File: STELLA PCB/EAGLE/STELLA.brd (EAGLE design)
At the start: 13.2 x 13.2 mm, 51 parts, among them Q1 ECS-.327-5-16-TR, T1 NXP_60_2N7002BKM, T2 NXP_60_2N7002BKM, T3 NXP_60_2N7002BKM, U1 PSSI2021SAY, U10 AD5142BCPZ100, U2 PSSI2021SAY, U4 SN74AUP1G06, U5 SN74AUP1G06, U6 MAX17220ENT+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

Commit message: update
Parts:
- C1, C2: value 4.7uF -> 4.7uF/6.3VDC
- C10, C3, C5, C7, C8, C9: value 0.1uF -> 0.1uF/6.3VDC
- C6, C6A: value 100uF -> 100uF/6.3VDC
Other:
- board text added: "1 - 8: Extension bus (optional)"
- board text removed: "1 - 8: Extension bus (nur optional)"
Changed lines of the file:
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@@
 <?xml version="1.0" encoding="utf-8"?>
 <!DOCTYPE eagle SYSTEM "eagle.dtd">
-<eagle version="9.4.2">
+<eagle version="9.6.2">
 <drawing>
 <settings>
@@
 <layers>
 <layer number="1" name="Top" color="4" fill="1" visible="yes" active="yes"/>
-<layer number="2" name="Route2" color="1" fill="3" visible="yes" active="yes"/>
-<layer number="3" name="Route3" color="4" fill="3" visible="yes" active="yes"/>
+<layer number="2" name="Route2" color="1" fill="3" visible="no" active="yes"/>
+<layer number="3" name="Route3" color="4" fill="3" visible="no" active="yes"/>
 <layer number="4" name="Route4" color="1" fill="4" visible="no" active="no"/>
 <layer number="5" name="Route5" color="4" fill="4" visible="no" active="no"/>
@@
 <layer number="24" name="bOrigins" color="15" fill="1" visible="yes" active="yes"/>
 <layer number="25" name="tNames" color="7" fill="1" visible="yes" active="yes"/>
-<layer number="26" name="bNames" color="7" fill="1" visible="yes" active="yes"/>
-<layer number="27" name="tValues" color="7" fill="1" visible="yes" active="yes"/>
-<layer number="28" name="bValues" color="7" fill="1" visible="yes" active="yes"/>
-<layer number="29" name="tStop" color="7" fill="3" visible="yes" active="yes"/>
-<layer number="30" name="bStop" color="7" fill="6" visible="yes" active="yes"/>
-<layer number="31" name="tCream" color="7" fill="4" visible="yes" active="yes"/>
-<layer number="32" name="bCream" color="7" fill="5" visible="yes" active="yes"/>
+<layer number="26" name="bNames" color="7" fill="1" visible="no" active="yes"/>
+<layer number="27" name="tValues" color="7" fill="1" visible="no" active="yes"/>
+<layer number="28" name="bValues" color="7" fill="1" visible="no" active="yes"/>
+<layer number="29" name="tStop" color="7" fill="3" visible="no" active="yes"/>
+<layer number="30" name="bStop" color="7" fill="6" visible="no" active="yes"/>
+<layer number="31" name="tCream" color="7" fill="4" visible="no" active="yes"/>
+<layer number="32" name="bCream" color="7" fill="5" visible="no" active="yes"/>
 <layer number="33" name="tFinish" color="6" fill="3" visible="no" active="yes"/>
 <layer number="34" name="bFinish" color="6" fill="6" visible="no" active="yes"/>
 <layer number="35" name="tGlue" color="7" fill="4" visible="no" active="yes"/>
 <layer number="36" name="bGlue" color="7" fill="5" visible="no" active="yes"/>
-<layer number="37" name="tTest" color="7" fill="1" visible="yes" active="yes"/>
-<layer number="38" name="bTest" color="7" fill="1" visible="yes" active="yes"/>
+<layer number="37" name="tTest" color="7" fill="1" visible="no" active="yes"/>
+<layer number="38" name="bTest" color="7" fill="1" visible="no" active="yes"/>
 <layer number="39" name="tKeepout" color="4" fill="11" visible="no" active="yes"/>
 <layer number="40" name="bKeepout" color="1" fill="11" visible="no" active="yes"/>
@@
 <layer number="42" name="bRestrict" color="1" fill="10" visible="no" active="yes"/>
 <layer number="43" name="vRestrict" color="2" fill="10" visible="no" active="yes"/>
-<layer number="44" name="Drills" color="7" fill="1" visible="yes" active="yes"/>
-<layer number="45" name="Holes" color="7" fill="1" visible="yes" active="yes"/>
-<layer number="46" name="Milling" color="3" fill="1" visible="yes" active="yes"/>
-<layer number="47" name="Measures" color="7" fill="1" visible="yes" active="yes"/>
+<layer number="44" name="Drills" color="7" fill="1" visible="no" active="yes"/>
+<layer number="45" name="Holes" color="7" fill="1" visible="no" active="yes"/>
+<layer number="46" name="Milling" color="3" fill="1" visible="no" active="yes"/>
+<layer number="47" name="Measures" color="7" fill="1" visible="no" active="yes"/>
 <layer number="48" name="Document" color="7" fill="1" visible="yes" active="yes"/>
 <layer number="49" name="Reference" color="7" fill="1" visible="yes" active="yes"/>
@@
 <text x="-10.55" y="-2.2" size="1.016" layer="105">16</text>
 <text x="-10.575" y="-3.5" size="1.016" layer="105">17</text>
-<text x="-19.4" y="-8.95" size="1.016" layer="105">1 - 8: Extension bus (nur optional)</text>
+<text x="-19.4" y="-8.95" size="1.016" layer="105">1 - 8: Extension bus (optional)</text>
 <text x="-19.55" y="-11.15" size="1.016" layer="105">13-16: Programming adapter 1.27 mm</text>
 </plain>
@@
 </autorouter>
 <elements>
-<element name="C1" library="UKN_rcl" package="C0402" value="4.7uF" x="1.47" y="4.23" smashed="yes" rot="MR0">
+<element name="C1" library="UKN_rcl" package="C0402" value="4.7uF/6.3VDC" x="1.47" y="4.23" smashed="yes" rot="MR0">
 <attribute name="NAME" x="0.78" y="4.115" size="0.254" layer="26" font="vector" rot="MR0"/>
 <attribute name="VALUE" x="0.805" y="4.1" size="0.3048" layer="28" rot="MR0"/>
 </element>
-<element name="C10" library="UKN_rcl" package="C0402" value="0.1uF" x="2.15" y="-2.35" smashed="yes" rot="MR270">
+<element name="C10" library="UKN_rcl" package="C0402" value="0.1uF/6.3VDC" x="2.15" y="-2.35" smashed="yes" rot="MR270">
 <attribute name="NAME" x="1.765" y="-1.385" size="0.254" layer="26" font="vector" rot="MR180"/>
 <attribute name="VALUE" x="1.69" y="-1.395" size="0.3048" layer="28" rot="MR180"/>
 </element>
-<element name="C2" library="UKN_rcl" package="C0402" value="4.7uF" x="1.5" y="5.05" smashed="yes" rot="MR0">
+<element name="C2" library="UKN_rcl" package="C0402" value="4.7uF/6.3VDC" x="1.5" y="5.05" smashed="yes" rot="MR0">
 <attribute name="NAME" x="0.785" y="4.96" size="0.254" layer="26" font="vector" rot="MR0"/>
 <attribute name="VALUE" x="0.81" y="4.87" size="0.3048" layer="28" rot="MR0"/>
 </element>
-<element name="C3" library="UKN_rcl" package="C0402" value="0.1uF" x="1.5" y="3.2" smashed="yes" rot="MR0">
+<element name="C3" library="UKN_rcl" package="C0402" value="0.1uF/6.3VDC" x="1.5" y="3.2" smashed="yes" rot="MR0">
 <attribute name="NAME" x="0.81" y="3.11" size="0.254" layer="26" font="vector" rot="MR0"/>
 <attribute name="VALUE" x="0.835" y="3.07" size="0.3048" layer="28" rot="MR0"/>
 </element>
-<element name="C5" library="UKN_rcl" package="C0402" value="0.1uF" x="-3.25" y="-4" smashed="yes" rot="MR180">
+<element name="C5" library="UKN_rcl" package="C0402" value="0.1uF/6.3VDC" x="-3.25" y="-4" smashed="yes" rot="MR180">
 <attribute name="NAME" x="-3.435" y="-4.385" size="0.254" layer="26" font="vector" rot="MR180"/>
 <attribute name="VALUE" x="-3.66" y="-4.47" size="0.3048" layer="28" rot="MR180"/>
 </element>
-<element name="C6" library="eZ430-RF2500T_HW-V1.0_20070403" package="RCL_C0805" value="100uF" x="-1.05" y="-3.75" smashed="yes" rot="MR90">
+<element name="C6" library="eZ430-RF2500T_HW-V1.0_20070403" package="RCL_C0805" value="100uF/6.3VDC" x="-1.05" y="-3.75" smashed="yes" rot="MR90">
 <attribute name="NAME" x="-1.215" y="-2.34" size="0.254" layer="26" font="vector" rot="MR180"/>
 <attribute name="VALUE" x="-1.685" y="-2.226" size="0.3048" layer="28" rot="MR180"/>
 </element>
-<element name="C6A" library="eZ430-RF2500T_HW-V1.0_20070403" package="RCL_C0805" value="100uF" x="0.6" y="-4.05" smashed="yes" rot="MR90">
+<element name="C6A" library="eZ430-RF2500T_HW-V1.0_20070403" package="RCL_C0805" value="100uF/6.3VDC" x="0.6" y="-4.05" smashed="yes" rot="MR90">
 <attribute name="NAME" x="0.28" y="-2.595" size="0.254" layer="26" font="vector" rot="MR180"/>
 <attribute name="VALUE" x="-0.035" y="-2.526" size="0.3048" layer="28" rot="MR180"/>
 </element>
-<element name="C7" library="UKN_rcl" package="C0402" value="0.1uF" x="1.5" y="2.4" smashed="yes" rot="MR0">
+<element name="C7" library="UKN_rcl" package="C0402" value="0.1uF/6.3VDC" x="1.5" y="2.4" smashed="yes" rot="MR0">
 <attribute name="NAME" x="0.81" y="2.31" size="0.254" layer="26" font="vector" rot="MR0"/>
 <attribute name="VALUE" x="0.785" y="2.295" size="0.3048" layer="28" rot="MR0"/>
 </element>
-<element name="C8" library="UKN_rcl" package="C0402" value="0.1uF" x="2.15" y="-4.85" smashed="yes" rot="MR270">
+<element name="C8" library="UKN_rcl" package="C0402" value="0.1uF/6.3VDC" x="2.15" y="-4.85" smashed="yes" rot="MR270">
 <attribute name="NAME" x="1.89" y="-3.96" size="0.254" layer="26" font="vector" rot="MR180"/>
 <attribute name="VALUE" x="1.59" y="-5.52" size="0.3048" layer="28" rot="MR180"/>
 </element>
-<element name="C9" library="UKN_rcl" package="C0402" value="0.1uF" x="-0.92" y="-0.96" smashed="yes" rot="MR180">
+<element name="C9" library="UKN_rcl" package="C0402" value="0.1uF/6.3VDC" x="-0.92" y="-0.96" smashed="yes" rot="MR180">
 <attribute name="NAME" x="-1.13" y="-0.32" size="0.254" layer="26" font="vector" rot="MR180"/>
 <attribute name="VALUE" x="-1.105" y="-0.28" size="0.3048" layer="28" rot="MR180"/>

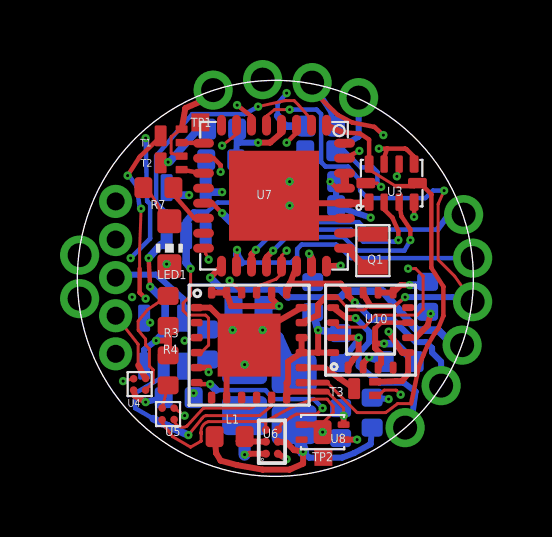
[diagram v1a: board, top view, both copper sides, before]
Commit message: - Move BIST measurement point for each channel to the node before the blocking capacitor - Add a 10 MΩ discharge resistor to each output channel - Replace 100 uF capacitors with 22 uF/16VDC versions - Fix several overlap and keepout violations - Improve routing and component placement - Include max voltage ratings in capacitor specs
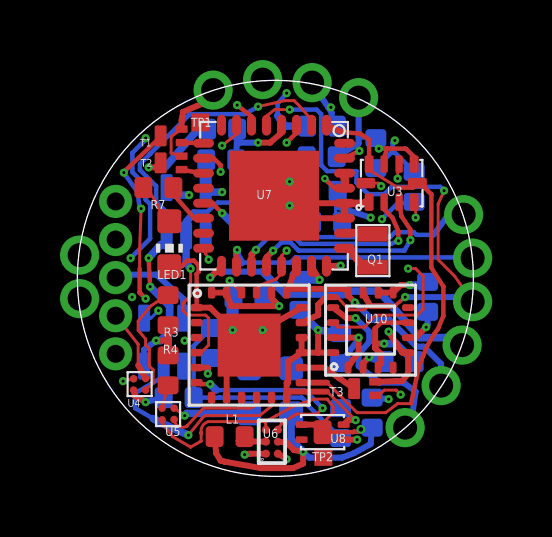
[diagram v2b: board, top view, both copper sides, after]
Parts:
- removed C6A: 100uF/6.3VDC, eZ430-RF2500T_HW-V1.0_20070403:RCL_C0805
- added C4: 22uF/16VDC, UKN_STELLA4_0_1_021022:MYRCL_0603
- added R11, R12: 10Meg/1%, UKN_rcl:R0402
- C6: value 100uF/6.3VDC -> 22uF/16VDC; device eZ430-RF2500T_HW-V1.0_20070403:RCL_C0805 -> UKN_STELLA4_0_1_021022:MYRCL_0603
- U8: value DRV5032AJDM -> DRV5032AJDM (FA)
- moved C7 0.59 mm to (1.70, 1.85)
- moved R1 0.43 mm to (0.80, -0.57)
- moved C3 0.33 mm to (1.55, 2.88)
- moved C9 0.30 mm to (-0.92, -0.66)
- moved C1 0.21 mm to (1.52, 4.03)
- moved C6 0.15 mm to (-0.90, -3.77), turned to 180 degrees
- moved R8 0.13 mm to (-2.15, -2.18)
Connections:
- net CURRENT_OUTPUT1: now also U3.10
- net CURRENT_OUTPUT2: now also U3.4
- net GND: now also C4.2, R11.1, R12.2; no longer C6A.2
- net STIM_OUT1: now also R11.2; no longer U3.10
- net STIM_OUT2: now also R12.1; no longer U3.4
- net VIN_BATT: now also C4.1; no longer C6A.1
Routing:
- net GND: track 43.3 -> 69.7 mm, vias 10 -> 8
- net CURRENT_OUTPUT1: track 10.4 -> 25.9 mm, vias 1 -> 2
- net CURRENT_OUTPUT2: track 32.8 -> 39.5 mm, vias 2 -> 3
- net STIM_OUT2: track 8.61 -> 11.8 mm
- net VCC: track 35.2 -> 37.4 mm
- net STIM_OUT1: track 5.02 -> 2.98 mm, vias 1 -> 0
- net N$3: track 2.08 -> 3.00 mm
- net VIN_BATT: track 30.3 -> 31.1 mm
- net PWM: track 15.6 -> 16.4 mm
- net _RST: track 8.06 -> 8.77 mm
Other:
- board text added: "1 bis 8: Aussenverbindung zur Funkplatine (nur optional)"
- board text added: "11,12: weiss, 10 cm Teflon"
- board text added: "13 bis 16: Programmieradapter 1,27 mm"
- board text added: "14/01/2020 ukn/DO"
- board text added: "17: rot, 10 cm Teflon"
- board text added: "9,10: schwarz 10cm Teflon"
- board text removed: "1 - 8: Extension bus (optional)"
- board text removed: "13-16: Programming adapter 1.27 mm"
